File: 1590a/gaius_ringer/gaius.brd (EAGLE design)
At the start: 33 x 33 mm, 30 parts, among them Q1 2N5088, Q2 2N3906, Q3 2N5088

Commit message: finished chorus and tremolo baords; other tweaks & polish
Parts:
- removed PAD1, PAD2, PAD5: PADSQR, supply pins:SQUARE
- removed PAD3, PAD4: PADRND, supply pins:ROUND
- added 9V: DC_MONO, jacks:DC
- added GND: PADRND, supply pins:ROUND
- added IN, OUT: PADSQR, supply pins:SQUARE
- C1, C3, C4, C5: device capacitors-film:BOX_SMALL -> capacitors-film:050X030_025_2
- D1: device diodes:DO41-2 -> diodes:DO41-3
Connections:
- removed net +9V: D1.A, PAD1.1
- removed net IN1: C1.2, PAD2.1, R1.2
- removed net OUT1: C5.1, PAD5.1, R13.2
- new net IN: C1.2, IN.1, R1.2
- new net N$13: 9V.T, D1.A
- new net OUT: C5.1, OUT.1, R13.2
- net GND: now also GND.1; no longer PAD3.1, PAD4.1
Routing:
- net IN: track 0.00 -> 10.8 mm
- net +9V: track 10.6 -> 0.00 mm
- net IN1: track 10.2 -> 0.00 mm
- net OUT: track 0.00 -> 9.57 mm
- net N$13: track 0.00 -> 8.89 mm
- net OUT1: track 8.04 -> 0.00 mm
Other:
- board size 33 x 33 mm -> 33 x 32.4 mm
- board text added: "(c) 2016 burr settles"
- board text added: "octavter + ring-modulator"
- board text removed: "+9V"
- board text removed: "GND"
- board text removed: "IN"
- board text removed: "OUT"
- board text removed: "octavter / ringmod (c) 2016 burr settles"
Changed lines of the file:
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@@
 <drawing>
 <settings>
-<setting alwaysvectorfont="no"/>
+<setting alwaysvectorfont="yes"/>
 <setting verticaltext="up"/>
 </settings>
@@
 <plain>
 <wire x1="0" y1="0" x2="33.02" y2="0" width="0" layer="20"/>
-<wire x1="33.02" y1="0" x2="33.02" y2="33.02" width="0" layer="20"/>
-<wire x1="33.02" y1="33.02" x2="0" y2="33.02" width="0" layer="20"/>
-<wire x1="0" y1="33.02" x2="0" y2="0" width="0" layer="20"/>
-<text x="22.86" y="3.81" size="1.27" layer="25" font="vector">GAIUS</text>
-<text x="22.86" y="1.905" size="0.508" layer="25" font="vector">octavter / ringmod
-(c) 2016 burr settles</text>
-<text x="13.335" y="1.27" size="0.8128" layer="25">IN</text>
-<text x="15.875" y="1.27" size="0.8128" layer="25">GND</text>
-<text x="19.05" y="1.27" size="0.8128" layer="25">OUT</text>
-<text x="28.575" y="30.48" size="0.8128" layer="25">GND</text>
-<text x="25.4" y="30.48" size="0.8128" layer="25">+9V</text>
+<wire x1="33.02" y1="0" x2="33.02" y2="32.385" width="0" layer="20"/>
+<wire x1="33.02" y1="32.385" x2="0" y2="32.385" width="0" layer="20"/>
+<wire x1="0" y1="32.385" x2="0" y2="0" width="0" layer="20"/>
+<text x="22.86" y="3.81" size="1.778" layer="25" font="vector">GAIUS</text>
+<text x="31.115" y="24.765" size="0.8128" layer="25" font="vector" align="bottom-right">(c) 2016
+burr settles</text>
+<text x="22.86" y="1.905" size="0.6096" layer="25" font="vector">octavter +
+ring-modulator</text>
 </plain>
 <attributes>
@@
 </autorouter>
 <elements>
-<element name="C1" library="capacitors-film" package="BOX_SMALL" value="47n" x="16.51" y="10.16" rot="R270"/>
-<element name="C3" library="capacitors-film" package="BOX_SMALL" value="47n" x="5.08" y="15.24"/>
-<element name="C4" library="capacitors-film" package="BOX_SMALL" value="47n" x="5.08" y="22.86" rot="R180"/>
+<element name="C1" library="capacitors-film" package="050X030_025_2" value="47n" x="16.51" y="10.16" rot="R270"/>
+<element name="C3" library="capacitors-film" package="050X030_025_2" value="47n" x="5.08" y="15.24"/>
+<element name="C4" library="capacitors-film" package="050X030_025_2" value="47n" x="5.08" y="22.86" rot="R180"/>
 <element name="C2" library="capacitors-elec" package="050_020_1" value="100u" x="21.59" y="27.94"/>
 <element name="D2" library="diodes" package="DO35-2" value="1N914" x="5.08" y="20.32" rot="R180"/>
 <element name="D3" library="diodes" package="DO35-2" value="1N914" x="5.08" y="17.78" rot="R180"/>
-<element name="D1" library="diodes" package="DO41-2" value="1N5817" x="14.605" y="29.845"/>
+<element name="D1" library="diodes" package="DO41-3" value="1N5817" x="14.605" y="29.845"/>
 <element name="NULL" library="potentiometers" package="2262_TRIM" value="25kB" x="5.08" y="28.575" rot="R180"/>
 <element name="Q1" library="transistors" package="TO92-" value="2N5088" x="19.685" y="15.24" rot="R90"/>
@@
 <element name="R9" library="resistors" package="R0207/3" value="68k" x="6.35" y="12.7"/>
 <element name="R8" library="resistors" package="R0207/3" value="68k" x="6.35" y="10.16" rot="R180"/>
-<element name="PAD1" library="supply pins" package="SQUARE" value="PADSQR" x="26.67" y="29.21" rot="R180"/>
-<element name="PAD2" library="supply pins" package="SQUARE" value="PADSQR" x="20.32" y="3.81"/>
-<element name="PAD5" library="supply pins" package="SQUARE" value="PADSQR" x="13.97" y="3.81"/>
-<element name="PAD3" library="supply pins" package="ROUND" value="PADRND" x="29.845" y="29.21" rot="R180"/>
-<element name="PAD4" library="supply pins" package="ROUND" value="PADRND" x="17.145" y="3.81"/>
-<element name="C5" library="capacitors-film" package="BOX_SMALL" value="100n" x="13.335" y="10.16" rot="R90"/>
+<element name="IN" library="supply pins" package="SQUARE" value="PADSQR" x="20.32" y="3.175"/>
+<element name="OUT" library="supply pins" package="SQUARE" value="PADSQR" x="15.24" y="3.175"/>
+<element name="GND" library="supply pins" package="ROUND" value="PADRND" x="17.78" y="3.175"/>
+<element name="C5" library="capacitors-film" package="050X030_025_2" value="100n" x="13.335" y="10.16" rot="R90"/>
+<element name="9V" library="jacks" package="DC" value="DC_MONO" x="28.575" y="29.845" rot="MR0"/>
 </elements>
 <signals>
@@
 <contactref element="R13" pad="1"/>
 <contactref element="R1" pad="1"/>
-<contactref element="PAD4" pad="1"/>
-<contactref element="PAD4" pad="1"/>
+<contactref element="GND" pad="1"/>
+<contactref element="GND" pad="1"/>
 <polygon width="0.254" layer="16">
-<vertex x="1.27" y="31.75"/>
-<vertex x="31.75" y="31.75"/>
+<vertex x="1.27" y="31.115"/>
+<vertex x="31.75" y="31.115"/>
 <vertex x="31.75" y="1.27"/>
 <vertex x="1.27" y="1.27"/>
 </polygon>
 <polygon width="0.254" layer="1">
-<vertex x="1.27" y="31.75"/>
-<vertex x="31.75" y="31.75"/>
+<vertex x="1.27" y="31.115"/>
+<vertex x="31.75" y="31.115"/>
 <vertex x="31.75" y="1.27"/>
 <vertex x="1.27" y="1.27"/>
 </polygon>
 <contactref element="C2" pad="-"/>
-<contactref element="PAD3" pad="1"/>
-<contactref element="PAD3" pad="1"/>
 </signal>
 <signal name="N$5">
@@
 <wire x1="7.62" y1="20.32" x2="7.62" y2="17.78" width="0.254" layer="1"/>
 </signal>
-<signal name="+9V">
-<contactref element="PAD1" pad="1"/>
-<contactref element="D1" pad="A"/>
-<wire x1="26.67" y1="29.21" x2="25.0825" y2="30.7975" width="0.6096" layer="1"/>
-<wire x1="25.0825" y1="30.7975" x2="18.0975" y2="30.7975" width="0.6096" layer="1"/>
-<wire x1="18.0975" y1="30.7975" x2="17.145" y2="29.845" width="0.6096" layer="1"/>
-</signal>
-<signal name="IN1">
+<signal name="IN">
 <contactref element="C1" pad="2"/>
 <contactref element="R1" pad="2"/>
-<contactref element="PAD2" pad="1"/>
-<wire x1="20.32" y1="3.81" x2="20.32" y2="7.62" width="0.254" layer="1"/>
+<contactref element="IN" pad="1"/>
+<wire x1="20.32" y1="3.175" x2="20.32" y2="7.62" width="0.254" layer="1"/>
 <wire x1="20.32" y1="7.62" x2="16.51" y2="7.62" width="0.254" layer="1"/>
 <wire x1="22.86" y1="7.62" x2="20.32" y2="7.62" width="0.254" layer="1"/>
 </signal>
-<signal name="OUT1">
+<signal name="OUT">
 <contactref element="R13" pad="2"/>
-<contactref element="PAD5" pad="1"/>
+<contactref element="OUT" pad="1"/>
 <contactref element="C5" pad="1"/>
 <wire x1="13.335" y1="7.62" x2="13.335" y2="4.445" width="0.254" layer="1"/>
-<wire x1="13.335" y1="4.445" x2="13.97" y2="3.81" width="0.254" layer="1"/>
 <wire x1="10.16" y1="2.54" x2="11.43" y2="2.54" width="0.254" layer="1"/>
 <wire x1="11.43" y1="2.54" x2="13.335" y2="4.445" width="0.254" layer="1"/>
+<wire x1="15.24" y1="3.175" x2="14.605" y2="3.175" width="0.254" layer="1"/>
+<wire x1="14.605" y1="3.175" x2="13.335" y2="4.445" width="0.254" layer="1"/>
 </signal>
 <signal name="N$12">
@@
 <wire x1="22.86" y1="25.4" x2="27.94" y2="25.4" width="0.6096" layer="1"/>
 <wire x1="30.48" y1="17.78" x2="30.48" y2="15.24" width="0.6096" layer="1"/>
-<wire x1="12.065" y1="29.845" x2="12.065" y2="27.94" width="0.6096" layer="1"/>
+<wire x1="10.795" y1="29.845" x2="12.065" y2="27.94" width="0.6096" layer="1"/>
 <wire x1="12.065" y1="27.94" x2="12.065" y2="26.67" width="0.6096" layer="1"/>
 <wire x1="11.43" y1="26.035" x2="12.065" y2="26.67" width="0.6096" layer="1"/>
@@
 <wire x1="30.48" y1="22.86" x2="27.94" y2="22.86" width="0.6096" layer="1"/>
 </signal>
+<signal name="N$13">
+<contactref element="D1" pad="A"/>
+<contactref element="9V" pad="T"/>
+<wire x1="27.305" y1="29.845" x2="18.415" y2="29.845" width="0.6096" layer="1"/>
+</signal>
 </signals>

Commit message: added RT logo; converted some pots trimmers
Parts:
- added U$1: (no value), logos:RT150
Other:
- board text added: "(c)2016 burr settles"
- board text removed: "(c) 2016 burr settles"
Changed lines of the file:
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@@
 <wire x1="33.02" y1="32.385" x2="0" y2="32.385" width="0" layer="20"/>
 <wire x1="0" y1="32.385" x2="0" y2="0" width="0" layer="20"/>
-<text x="22.86" y="3.81" size="1.778" layer="25" font="vector">GAIUS</text>
-<text x="31.115" y="24.765" size="0.8128" layer="25" font="vector" align="bottom-right">(c) 2016
+<text x="22.86" y="3.302" size="2.1844" layer="25" font="vector">GAIUS</text>
+<text x="31.115" y="24.638" size="0.8128" layer="25" font="vector" align="bottom-right">(c)2016
 burr settles</text>
-<text x="22.86" y="1.905" size="0.6096" layer="25" font="vector">octavter +
+<text x="22.86" y="0.889" size="0.762" layer="25" font="vector">octavter +
 ring-modulator</text>
 </plain>
@@
 <element name="C5" library="capacitors-film" package="050X030_025_2" value="100n" x="13.335" y="10.16" rot="R90"/>
 <element name="9V" library="jacks" package="DC" value="DC_MONO" x="28.575" y="29.845" rot="MR0"/>
+<element name="U$1" library="logos" package="RT150" value="" x="9.398" y="14.732"/>
 </elements>
 <signals>

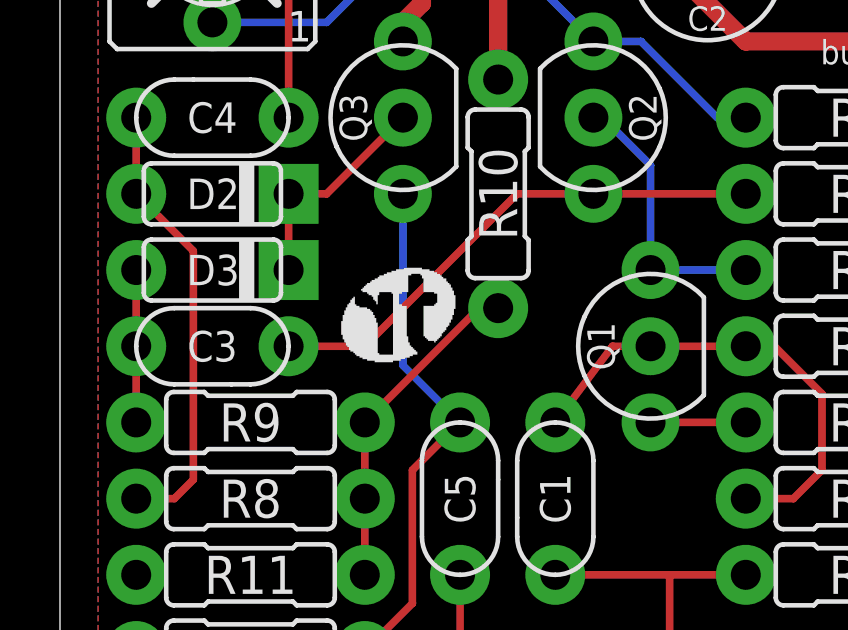
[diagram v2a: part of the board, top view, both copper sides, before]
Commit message: convert bitmap logos to polygons
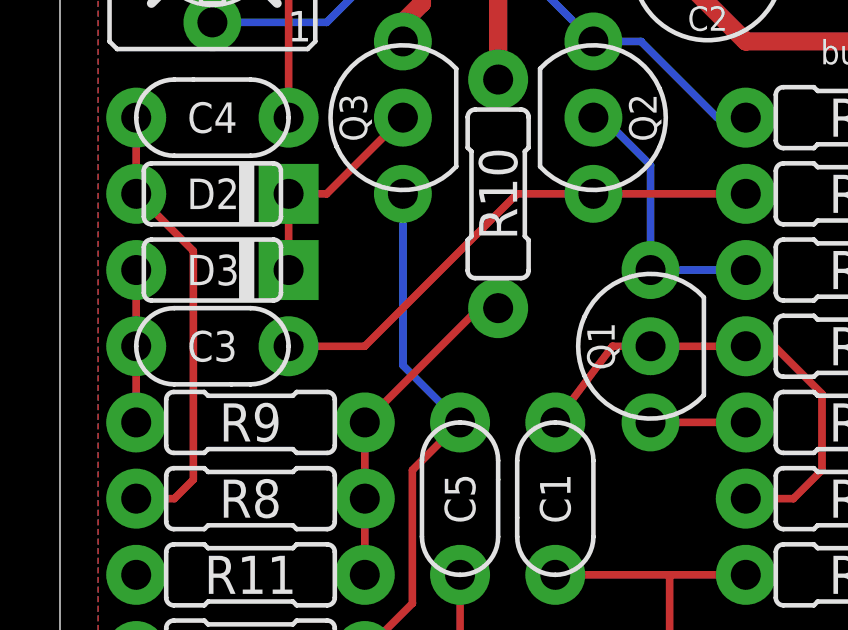
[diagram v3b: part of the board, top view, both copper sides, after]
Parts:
- U$1: device logos:RT150 -> logos:RT0150
- moved U$1 2.43 mm to (11.0, 16.5)
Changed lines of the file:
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@@
 <element name="C5" library="capacitors-film" package="050X030_025_2" value="100n" x="13.335" y="10.16" rot="R90"/>
 <element name="9V" library="jacks" package="DC" value="DC_MONO" x="28.575" y="29.845" rot="MR0"/>
-<element name="U$1" library="logos" package="RT150" value="" x="9.398" y="14.732"/>
+<element name="U$1" library="logos" package="RT0150" value="" x="11.049" y="16.51"/>
 </elements>
 <signals>
